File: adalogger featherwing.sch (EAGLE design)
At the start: 18 parts, among them IC1 RTC_PCF8523T, SW1 KMR2, X4 microsd, Y1 32khz

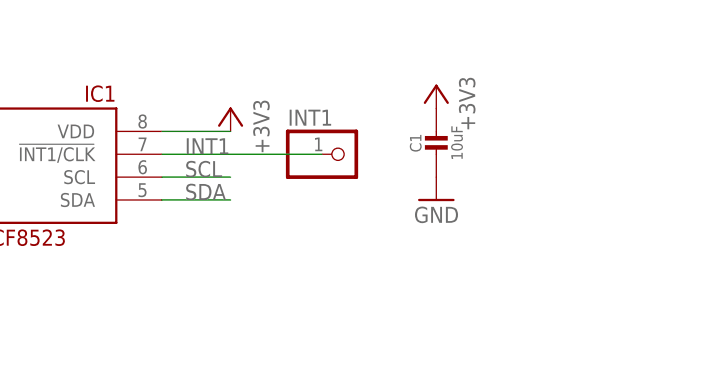
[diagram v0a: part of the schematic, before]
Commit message: added RC network on PCF vdd line
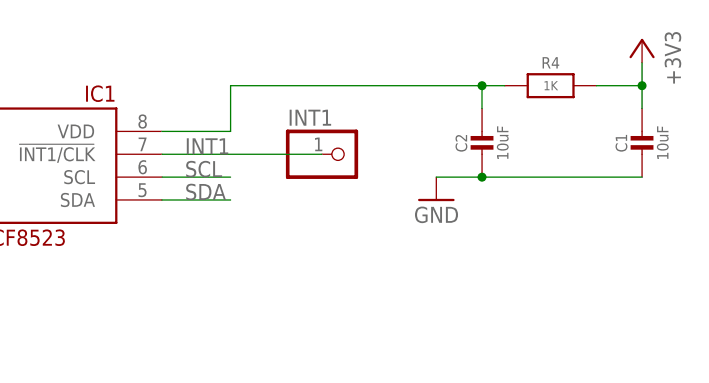
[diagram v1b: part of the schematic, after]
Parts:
- added C2: 10uF, microbuilder:CAP_CERAMIC0805-NOOUTLINE
- added R4: 1K, microbuilder:RESISTOR0805_NOOUTLINE
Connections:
- new net PCFVDD: C2.1, IC1.VDD, R4.2
- net +3V3: now also R4.1; no longer IC1.VDD
- net GND: now also C2.2
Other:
- moved on the sheet: C1
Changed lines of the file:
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@@
 <?xml version="1.0" encoding="utf-8"?>
 <!DOCTYPE eagle SYSTEM "eagle.dtd">
-<eagle version="6.4">
+<eagle version="7.5.0">
 <drawing>
 <settings>
@@
 <part name="IC1" library="microbuilder" deviceset="RTC_PCF8523" device="T"/>
 <part name="Y1" library="microbuilder" deviceset="CRYSTAL" device="8.0X3.8" value="32khz"/>
-<part name="+3V2" library="supply1" deviceset="+3V3" device=""/>
 <part name="R1" library="microbuilder" deviceset="RESISTOR" device="0805_NOOUTLINE" value="10K"/>
 <part name="R2" library="microbuilder" deviceset="RESISTOR" device="0805_NOOUTLINE" value="10K"/>
@@
 <part name="FID1" library="microbuilder" deviceset="FIDUCIAL" device="&quot;&quot;"/>
 <part name="FID2" library="microbuilder" deviceset="FIDUCIAL" device="&quot;&quot;"/>
+<part name="R4" library="microbuilder" deviceset="RESISTOR" device="0805_NOOUTLINE" value="1K"/>
+<part name="C2" library="microbuilder" deviceset="CAP_CERAMIC" device="0805-NOOUTLINE" value="10uF"/>
 </parts>
 <sheets>
@@
 <instance part="IC1" gate="G$1" x="182.88" y="160.02"/>
 <instance part="Y1" gate="G$1" x="160.02" y="162.56" rot="MR90"/>
-<instance part="+3V2" gate="G$1" x="205.74" y="165.1" rot="MR0"/>
 <instance part="R1" gate="G$1" x="73.66" y="116.84" rot="R90"/>
 <instance part="R2" gate="G$1" x="71.12" y="116.84" rot="R90"/>
@@
 <instance part="GND3" gate="1" x="167.64" y="149.86" rot="MR0"/>
 <instance part="GND4" gate="1" x="162.56" y="127" rot="MR0"/>
-<instance part="C1" gate="G$1" x="228.6" y="160.02"/>
-<instance part="+3V6" gate="G$1" x="228.6" y="167.64" rot="MR0"/>
+<instance part="C1" gate="G$1" x="251.46" y="160.02"/>
+<instance part="+3V6" gate="G$1" x="251.46" y="172.72" rot="MR0"/>
 <instance part="GND5" gate="1" x="228.6" y="154.94" rot="MR0"/>
 <instance part="JP1" gate="G$1" x="60.96" y="99.06" rot="R90"/>
@@
 <instance part="FID1" gate="G$1" x="241.3" y="25.4"/>
 <instance part="FID2" gate="G$1" x="241.3" y="30.48"/>
+<instance part="R4" gate="G$1" x="241.3" y="167.64" rot="MR0"/>
+<instance part="C2" gate="G$1" x="233.68" y="160.02"/>
 </instances>
 <busses>
@@
 <pinref part="C1" gate="G$1" pin="2"/>
 <pinref part="GND5" gate="1" pin="GND"/>
+<wire x1="251.46" y1="157.48" x2="233.68" y2="157.48" width="0.1524" layer="91"/>
+<pinref part="C2" gate="G$1" pin="2"/>
+<junction x="233.68" y="157.48"/>
+<wire x1="233.68" y1="157.48" x2="228.6" y2="157.48" width="0.1524" layer="91"/>
 </segment>
 </net>
@@
 <wire x1="38.1" y1="25.4" x2="38.1" y2="38.1" width="0.1524" layer="91"/>
 <wire x1="38.1" y1="25.4" x2="38.1" y2="10.16" width="0.1524" layer="91"/>
-</segment>
-<segment>
-<pinref part="IC1" gate="G$1" pin="VDD"/>
-<pinref part="+3V2" gate="G$1" pin="+3V3"/>
-<wire x1="205.74" y1="162.56" x2="198.12" y2="162.56" width="0.1524" layer="91"/>
 </segment>
 <segment>
@@
 <pinref part="C1" gate="G$1" pin="1"/>
 <pinref part="+3V6" gate="G$1" pin="+3V3"/>
+<wire x1="251.46" y1="170.18" x2="251.46" y2="167.64" width="0.1524" layer="91"/>
+<pinref part="R4" gate="G$1" pin="1"/>
+<wire x1="251.46" y1="167.64" x2="251.46" y2="165.1" width="0.1524" layer="91"/>
+<wire x1="246.38" y1="167.64" x2="251.46" y2="167.64" width="0.1524" layer="91"/>
+<junction x="251.46" y="167.64"/>
 </segment>
 </net>
@@
 </segment>
 </net>
+<net name="PCFVDD" class="0">
+<segment>
+<pinref part="IC1" gate="G$1" pin="VDD"/>
+<wire x1="198.12" y1="162.56" x2="205.74" y2="162.56" width="0.1524" layer="91"/>
+<pinref part="R4" gate="G$1" pin="2"/>
+<wire x1="205.74" y1="162.56" x2="205.74" y2="167.64" width="0.1524" layer="91"/>
+<wire x1="205.74" y1="167.64" x2="233.68" y2="167.64" width="0.1524" layer="91"/>
+<pinref part="C2" gate="G$1" pin="1"/>
+<wire x1="233.68" y1="167.64" x2="236.22" y2="167.64" width="0.1524" layer="91"/>
+<wire x1="233.68" y1="165.1" x2="233.68" y2="167.64" width="0.1524" layer="91"/>
+<junction x="233.68" y="167.64"/>
+</segment>
+</net>
